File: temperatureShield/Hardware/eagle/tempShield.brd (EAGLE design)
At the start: 59.7 x 31.8 mm, 33 parts, among them U1 SHT30, U2 TMP007, U3 FUJITSU_MB85RS1MT

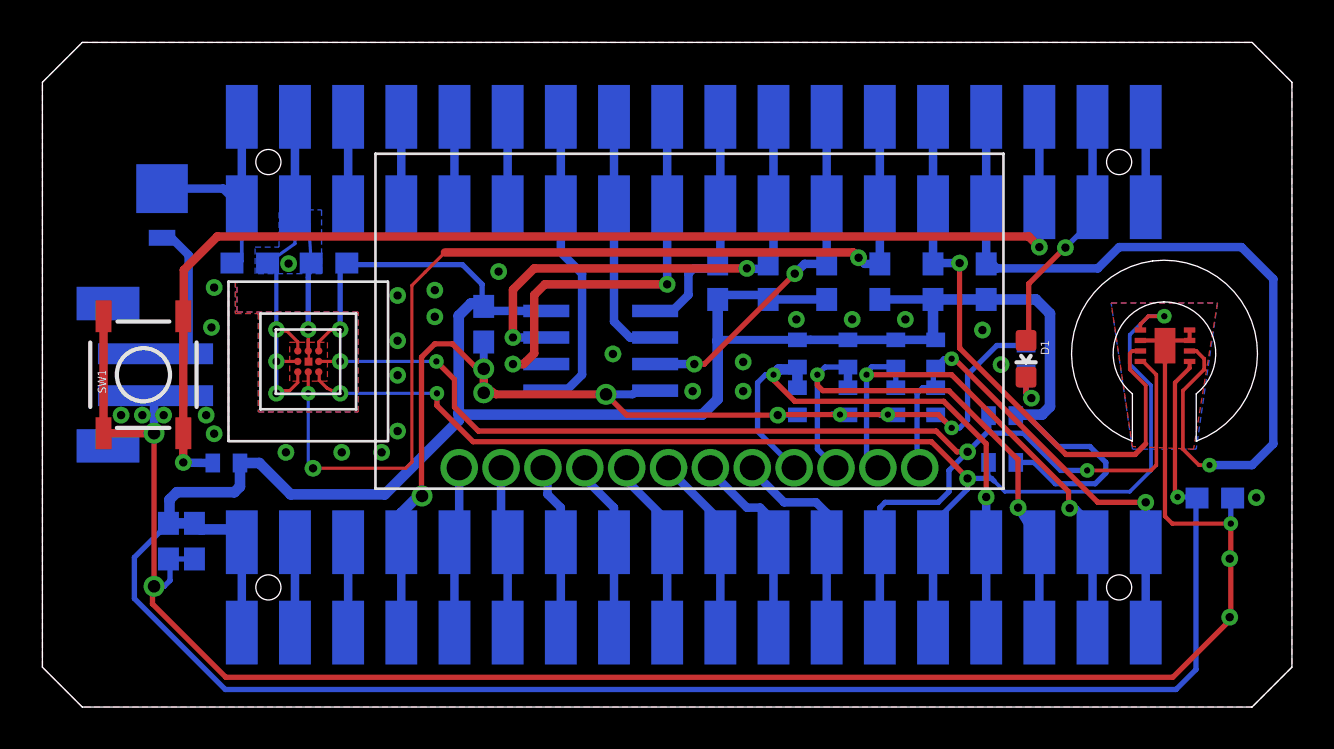
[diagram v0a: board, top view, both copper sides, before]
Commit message: change the pad for BGA chip and generate the gerber
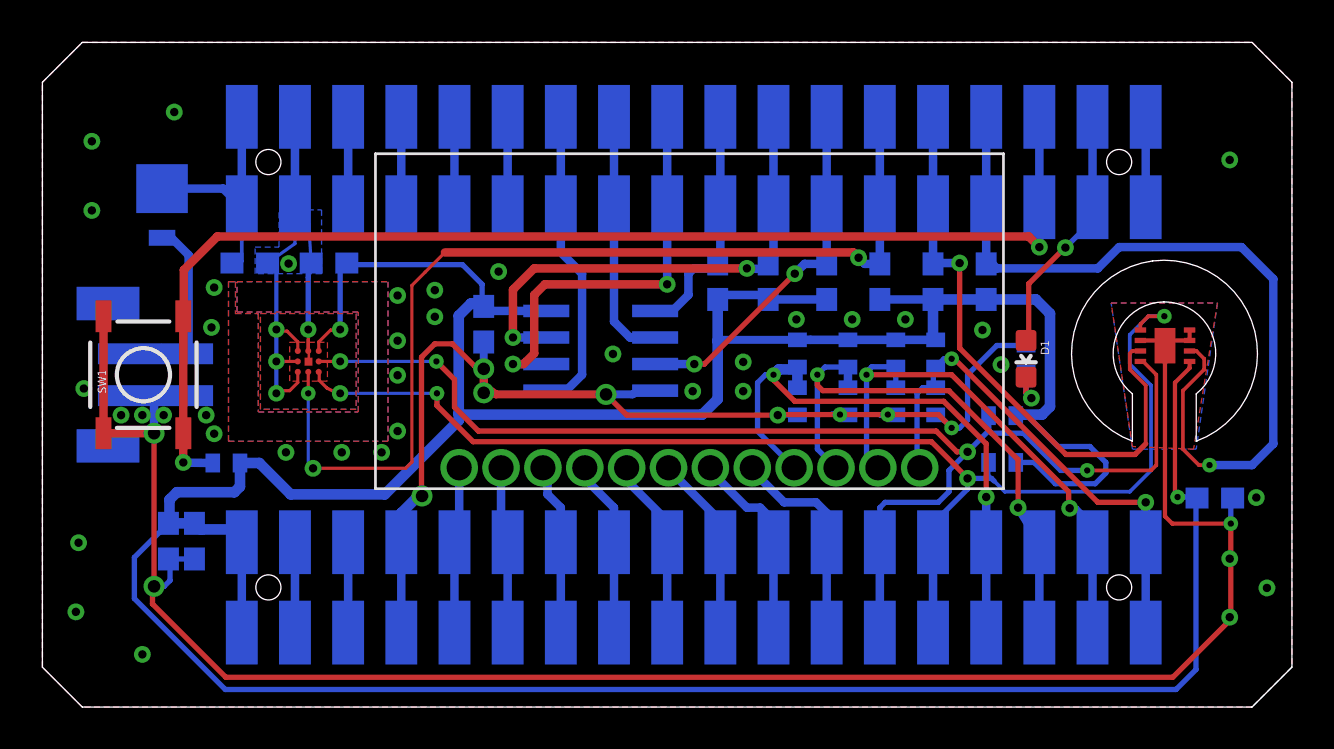
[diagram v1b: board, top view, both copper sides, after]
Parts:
- U2: device Particle:TMP007 -> Particle:TMP007_1
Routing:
- net GND: vias 45 -> 54
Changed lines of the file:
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@@
 <wire x1="55.118" y1="14.9606" x2="55.118" y2="12.7" width="0.05" layer="20"/>
 <wire x1="52.07" y1="14.9606" x2="52.07" y2="12.7" width="0.05" layer="20"/>
-<wire x1="16.51" y1="20.32" x2="16.51" y2="12.7254" width="0.127" layer="21"/>
-<wire x1="8.89" y1="20.32" x2="8.89" y2="12.7254" width="0.127" layer="21"/>
-<wire x1="8.89" y1="20.32" x2="16.4846" y2="20.32" width="0.127" layer="21"/>
-<wire x1="8.89" y1="12.7" x2="16.51" y2="12.7" width="0.127" layer="21"/>
-<wire x1="11.1506" y1="18.034" x2="14.224" y2="18.034" width="0.127" layer="21"/>
-<wire x1="14.224" y1="18.034" x2="14.224" y2="14.9606" width="0.127" layer="21"/>
-<wire x1="14.224" y1="14.9606" x2="11.1506" y2="14.9606" width="0.127" layer="21"/>
-<wire x1="11.1506" y1="14.9606" x2="11.1506" y2="18.034" width="0.127" layer="21"/>
-<wire x1="10.414" y1="18.796" x2="14.986" y2="18.796" width="0.127" layer="21"/>
-<wire x1="14.986" y1="18.796" x2="14.986" y2="14.224" width="0.127" layer="21"/>
-<wire x1="14.986" y1="14.224" x2="10.414" y2="14.224" width="0.127" layer="21"/>
-<wire x1="10.414" y1="14.224" x2="10.414" y2="18.796" width="0.127" layer="21"/>
 <rectangle x1="12.5222" y1="16.3068" x2="12.9032" y2="16.6878" layer="1"/>
 </plain>
@@
 <param name="mlMinCreamFrame" value="0mil"/>
 <param name="mlMaxCreamFrame" value="0mil"/>
-<param name="mlViaStopLimit" value="0mil"/>
+<param name="mlViaStopLimit" value="0.7mm"/>
 <param name="srRoundness" value="0"/>
 <param name="srMinRoundness" value="0mil"/>
@@
 <attribute name="U" value="" x="52.451" y="16.51" size="1.778" layer="27" display="off"/>
 </element>
-<element name="U2" library="Particle" package="TMP007" value="TMP007" x="12.7" y="16.51"/>
+<element name="U2" library="Particle" package="TMP007_1" value="TMP007" x="12.7" y="16.51"/>
 <element name="U4" library="Particle" package="LCD" value="" x="41.91" y="11.43" rot="R180"/>
 <element name="R6" library="SparkFun-Resistors" package="0603-RES" value="10k" x="42.545" y="20.32" rot="MR270">
@@
 </polygon>
 <via x="11.7602" y="21.1836" extent="1-16" drill="0.4" diameter="0.5"/>
+<via x="4.7752" y="2.5146" extent="1-16" drill="0.4" diameter="0.5"/>
+<via x="1.6002" y="4.5466" extent="1-16" drill="0.4" diameter="0.5"/>
+<via x="1.7272" y="7.8486" extent="1-16" drill="0.4" diameter="0.5"/>
+<via x="1.9812" y="15.2146" extent="1-16" drill="0.4" diameter="0.5"/>
+<via x="2.3622" y="23.7236" extent="1-16" drill="0.4" diameter="0.5"/>
+<via x="2.3622" y="27.0256" extent="1-16" drill="0.4" diameter="0.5"/>
+<via x="6.2992" y="28.4226" extent="1-16" drill="0.4" diameter="0.5"/>
+<via x="56.7182" y="26.1366" extent="1-16" drill="0.4" diameter="0.5"/>
+<via x="58.4962" y="5.6896" extent="1-16" drill="0.4" diameter="0.5"/>
 </signal>
 <signal name="!CS">
